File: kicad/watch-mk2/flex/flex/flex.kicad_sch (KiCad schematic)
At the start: 7 parts, among them P1 AXT510124, Q1 Si1308EDL, SW1 MCSLPT4644B4PHTR, SW2 MCSLPT4644B4PHTR

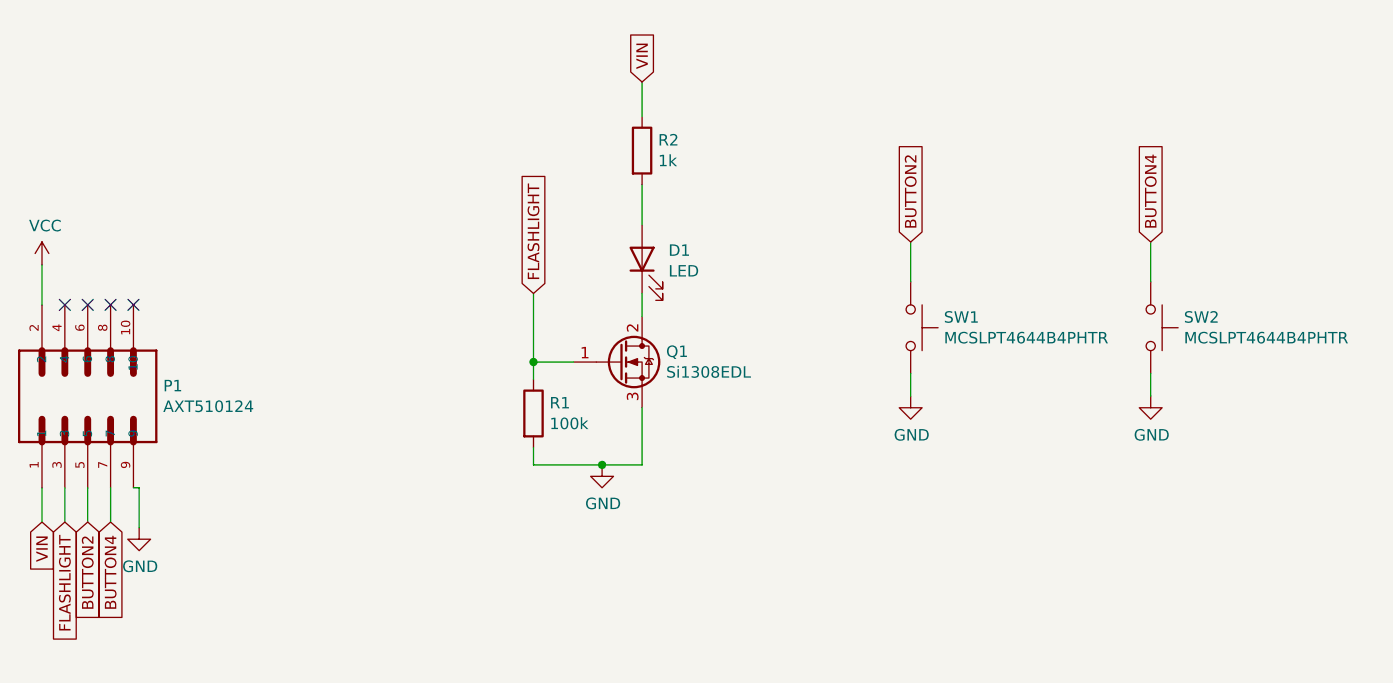
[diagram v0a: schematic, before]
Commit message: add rev2 of flex cable
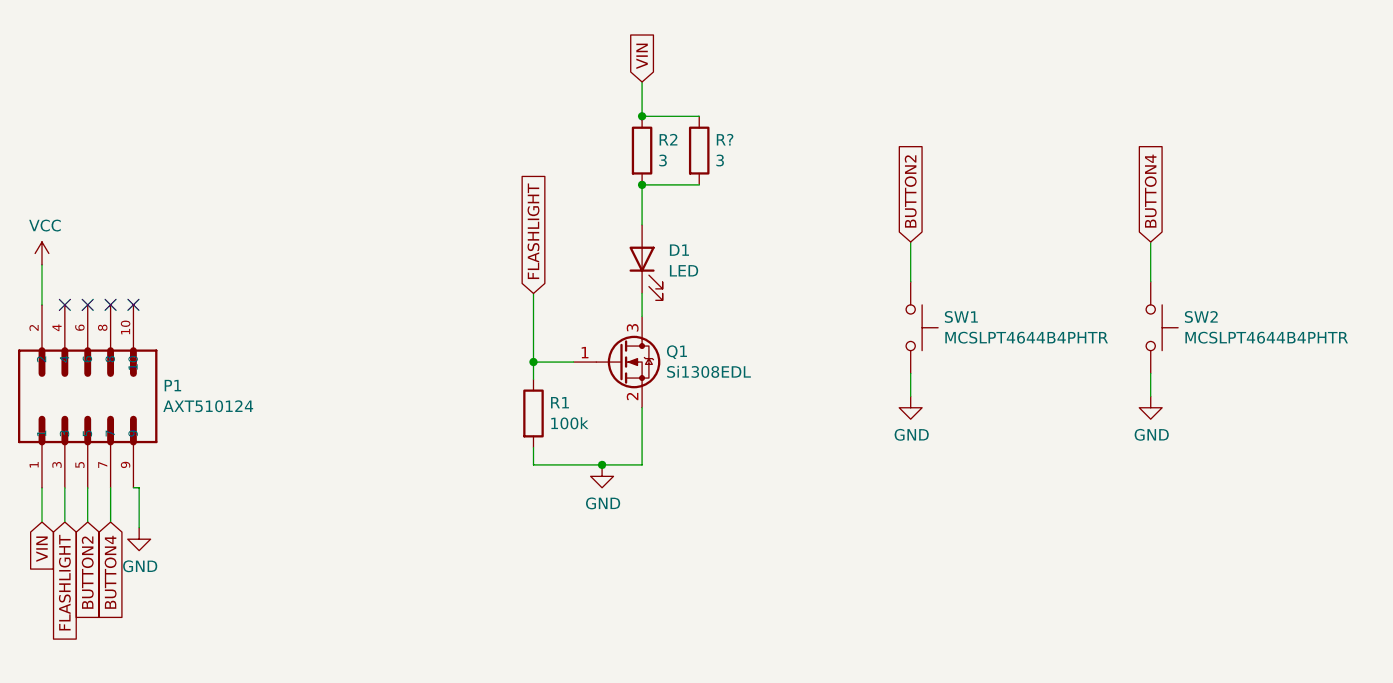
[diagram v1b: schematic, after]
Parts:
- added R?: 3, Resistor_SMD:R_0603_1608Metric, symbol Device:R
- Q1: symbol Device:Q_NMOS_GDS -> Device:Q_NMOS_GSD
- R2: value 1k -> 3; footprint Resistor_SMD:R_0603_1608Metric_Pad1.05x0.95mm_HandSolder -> Resistor_SMD:R_2512_6332Metric
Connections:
- net GND: now also Q1.2 (S); no longer Q1.3 (S)
- net VIN: now also R?.1
- net at D1.2 (A), R2.2: now also R?.2
- net at D1.1 (K): now also Q1.3 (D); no longer Q1.2 (D)
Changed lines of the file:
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@@
   (junction (at 107.95 87.63) (diameter 0) (color 0 0 0 0))
   (junction (at 115.57 99.06) (diameter 0) (color 0 0 0 0))
+  (junction (at 120.015 60.325) (diameter 0) (color 0 0 0 0))
+  (junction (at 120.015 67.945) (diameter 0) (color 0 0 0 0))
+  (no_connect (at 60.96 81.28))
+  (no_connect (at 58.42 81.28))
   (no_connect (at 55.88 81.28))
   (no_connect (at 63.5 81.28))
-  (no_connect (at 60.96 81.28))
-  (no_connect (at 58.42 81.28))
   (wire (pts (xy 53.34 76.835) (xy 53.34 81.28))
     (stroke (width 0) (type solid) (color 0 0 0 0))
@@
     (stroke (width 0) (type solid) (color 0 0 0 0))
   )
+  (wire (pts (xy 120.015 60.325) (xy 126.365 60.325))
+    (stroke (width 0) (type solid) (color 0 0 0 0))
+  )
   (wire (pts (xy 120.015 67.945) (xy 120.015 72.39))
+    (stroke (width 0) (type solid) (color 0 0 0 0))
+  )
+  (wire (pts (xy 120.015 67.945) (xy 126.365 67.945))
     (stroke (width 0) (type solid) (color 0 0 0 0))
   )
@@
       (effects (font (size 1.27 1.27)) (justify left))
     )
-    (property "Value" "1k" (id 1) (at 121.793 65.284 0)
-      (effects (font (size 1.27 1.27)) (justify left))
-    )
-    (property "Footprint" "Resistor_SMD:R_0603_1608Metric_Pad1.05x0.95mm_HandSolder" (id 2) (at 118.237 64.135 90)
+    (property "Value" "3" (id 1) (at 121.793 65.284 0)
+      (effects (font (size 1.27 1.27)) (justify left))
+    )
+    (property "Footprint" "Resistor_SMD:R_2512_6332Metric" (id 2) (at 118.237 64.135 90)
       (effects (font (size 1.27 1.27)) hide)
     )
     (property "Datasheet" "~" (id 3) (at 120.015 64.135 0)
+      (effects (font (size 1.27 1.27)) hide)
+    )
+  )
+  (symbol (lib_id "Device:R") (at 126.365 64.135 0) (unit 1)
+    (in_bom yes) (on_board yes)
+    (property "Reference" "R?" (id 0) (at 128.1431 62.9856 0)
+      (effects (font (size 1.27 1.27)) (justify left))
+    )
+    (property "Value" "3" (id 1) (at 128.143 65.284 0)
+      (effects (font (size 1.27 1.27)) (justify left))
+    )
+    (property "Footprint" "Resistor_SMD:R_0603_1608Metric" (id 2) (at 124.587 64.135 90)
+      (effects (font (size 1.27 1.27)) hide)
+    )
+    (property "Datasheet" "~" (id 3) (at 126.365 64.135 0)
       (effects (font (size 1.27 1.27)) hide)
     )
@@
     )
   )
-  (symbol (lib_id "Device:Q_NMOS_GDS") (at 117.475 87.63 0) (unit 1)
+  (symbol (lib_id "Device:Q_NMOS_GSD") (at 117.475 87.63 0) (unit 1)
     (in_bom yes) (on_board yes)
     (property "Reference" "Q1" (id 0) (at 122.6821 86.4806 0)
@@
       (reference "R2") (unit 1)
     )
+    (path "/e3642b18-fe7f-49e6-aba7-825f27d6e656"
+      (reference "R?") (unit 1)
+    )
     (path "/a7e76ac4-6608-467a-82aa-a60c16cb0165"

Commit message: checkpoint
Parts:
- gave numbers to parts that had none: 1
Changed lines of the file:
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@@
   (symbol (lib_id "Device:R") (at 126.365 64.135 0) (unit 1)
     (in_bom yes) (on_board yes)
-    (property "Reference" "R?" (id 0) (at 128.1431 62.9856 0)
+    (property "Reference" "R3" (id 0) (at 128.1431 62.9856 0)
       (effects (font (size 1.27 1.27)) (justify left))
     )
@@
     )
     (path "/e3642b18-fe7f-49e6-aba7-825f27d6e656"
-      (reference "R?") (unit 1)
+      (reference "R3") (unit 1)
     )
     (path "/a7e76ac4-6608-467a-82aa-a60c16cb0165"
